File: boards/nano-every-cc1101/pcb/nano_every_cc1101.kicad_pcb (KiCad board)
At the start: 2 copper layers, 100 x 100 mm, 86 parts, among them J1 SMA, J2 SMA, J3 Breakout 1-15, J4 Breakout 16-30, U1 CC1101RGPR, U2 XC6206P332MR, U3 TXS0108EPWR, U501 CC1101RGPR, Y1 26MHz, Y501 26MHz

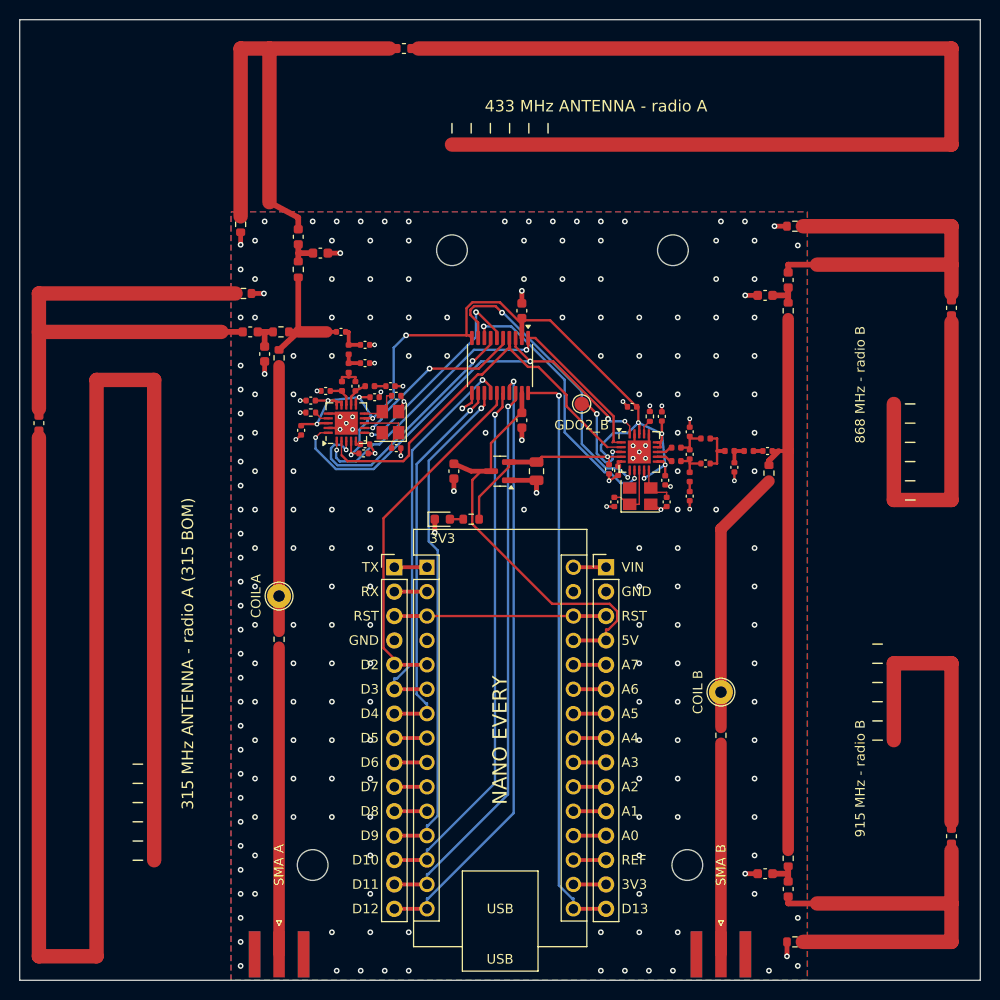
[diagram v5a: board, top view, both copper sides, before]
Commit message: nano-every-cc1101 v2: 70 x 45 mm board with JLCPCB-assembled coil antennas
- Printed IFAs replaced by four helical spring antennas (BAT WIRELESS
  BWxxxSNX, 315/433/868/915 MHz, LCSC C496553-C496556), all fitted and
  assembled; one 0R selector per radio picks the band, each branch keeps a
  T-match for retuning, SMA jacks stay as a hand-fit option.
- Board shrinks from 100 x 100 to 70 x 45 mm: radios stacked beside the
  Nano, TXS0108E rotated so its 5 V side faces the Nano.
- DRC now 0 violations / 0 unconnected: footprint silk clipped off pads
  and the board edge, C41/C51 moved so the DCOUPL cap clears the QFN body,
  a .kicad_dru rule for the intentional QFN-courtyard contacts, ground
  corridors kept open for the CC1101 exposed pads, ground-island joining,
  orphan via stubs removed.
- Docs rewritten for the coil version; antenna/ kept as the v1 study.

Co-Authored-By: Claude Opus 5.5 <noreply@anthropic.com>
Claude-Session: https://claude.ai/code/session_019aUkwoH7eUuCGWSrK9KSBc
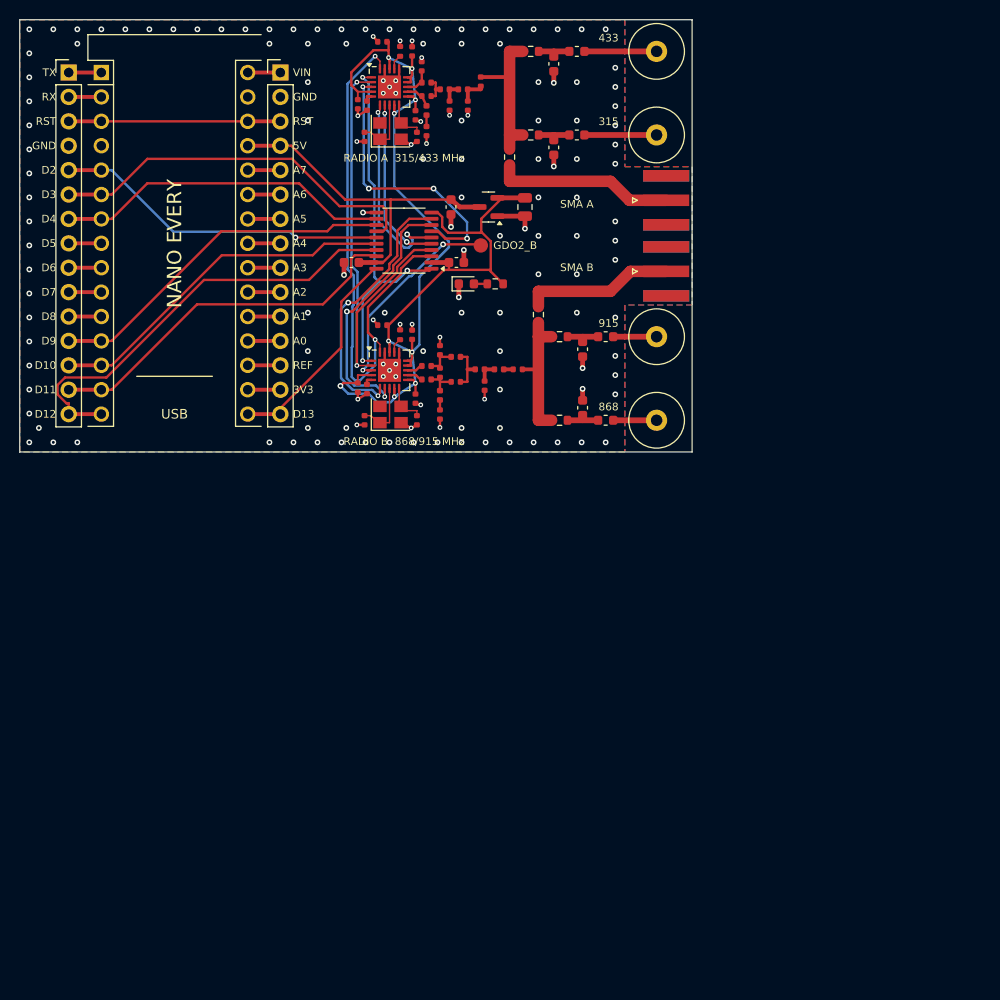
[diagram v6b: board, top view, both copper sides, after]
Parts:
- removed H1, H2: coil, TestPoint:TestPoint_THTPad_D2.5mm_Drill1.2mm
- removed H3, H4, H5, H6: M3, MountingHole:MountingHole_3.2mm_M3
- removed L401: 47pF, Inductor_SMD:L_0603_1608Metric
- removed L402: DNP (39nH to use), Inductor_SMD:L_0603_1608Metric
- removed L404, L405: 0R, Inductor_SMD:L_0603_1608Metric
- removed R401, R402, R404, R405: 0R, Resistor_SMD:R_0603_1608Metric
- removed R407, R408: DNP, Resistor_SMD:R_0603_1608Metric
- added AE1: BW433SNX21-5W2, nano_every_cc1101:Coil_Spring_D5.5_THT, F.Cu at (166.3, 103.3)
- added AE2: BW315SNX39-6W3, nano_every_cc1101:Coil_Spring_D5.5_THT, F.Cu at (166.3, 112.0)
- added AE3: BW868SNX20-5Z6, nano_every_cc1101:Coil_Spring_D5.5_THT, F.Cu at (166.3, 141.7)
- added AE4: BW915SNX17-5W2, nano_every_cc1101:Coil_Spring_D5.5_THT, F.Cu at (166.3, 133.0)
- C301, C321, C331: value 3pF -> DNP
- C311: value 47pF -> DNP
- L301, L321: value 6pF -> 0R
- L311: value 18pF -> 0R
- L331: value 3pF -> 0R
- R311, R331: value DNP (0R to use) -> DNP
- moved J1 88.2 mm to (167.3, 118.8), turned to 0 degrees
- moved J2 71.3 mm to (167.3, 126.2), turned to 0 degrees
- moved A1 61.7 mm to (108.5, 105.5)
- moved J3 61.7 mm to (105.1, 105.5)
- moved J4 61.7 mm to (127.1, 105.5)
- moved L331 60.6 mm to (161.0, 133.0), turned to 0 degrees
- moved R331 59.3 mm to (156.2, 133.0), turned to 0 degrees
- moved C331 57.8 mm to (158.6, 134.3), turned to 90 degrees
- moved C181 41.3 mm to (137.8, 102.3), turned to 0 degrees
- moved L311 39.7 mm to (158.0, 112.0)
- moved R171 38.7 mm to (139.6, 103.3), turned to 90 degrees
- moved C151 37.9 mm to (140.8, 103.3), turned to 90 degrees
- moved C311 37.0 mm to (155.6, 113.3)
- moved C41 36.4 mm to (135.2, 108.8), turned to 90 degrees
- moved U1 35.3 mm to (138.5, 107.0), turned to 0 degrees
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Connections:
- C301 pad 1: M_433 -> GND
- C301 pad 2: GND -> M_433
- C321 pad 1: GND -> M_868
- C321 pad 2: M_868 -> GND
- L311 pad 1: FEED_315 -> M_315
- L311 pad 2: M_315 -> FEED_315
- L331 pad 1: FEED_915 -> M_915
- L331 pad 2: M_915 -> FEED_915
- R311 pad 1: M_315 -> ANT_A
- R311 pad 2: ANT_A -> M_315
- R331 pad 1: M_915 -> ANT_B
- R331 pad 2: ANT_B -> M_915
- R403 pad 1: EXT_A -> SMA_A
- R406 pad 1: EXT_B -> ANT_B
- R406 pad 2: ANT_B -> SMA_B
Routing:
- net ARM_315: track 176.7 -> 0.00 mm
- net ARM_433: track 118.2 -> 0.00 mm
- net FEED_315: track 54.4 -> 7.51 mm
- net FEED_433: track 54.3 -> 7.51 mm
- net ANT_B: track 58.9 -> 14.6 mm
- net FEED_915: track 43.4 -> 4.51 mm
- net D13_SCK: track 60.8 -> 23.1 mm, vias 1 -> 0
- net FEED_868: track 41.0 -> 4.51 mm
- net ARM_868: track 35.2 -> 0.00 mm
- net ARM_915: track 31.2 -> 0.00 mm
- net EXT_B: track 27.7 -> 0.00 mm
- net EXT_A: track 27.7 -> 0.00 mm
- net D11_MOSI: track 58.5 -> 38.9 mm, vias 1 -> 0
- net D10: track 55.4 -> 37.3 mm, vias 1 -> 0
- net D12_MISO: track 63.5 -> 46.1 mm, vias 1 -> 0
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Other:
- board size 100 x 100 mm -> 70 x 45 mm
- board text added: "2-layer 70 x 45 mm v2.0 coil antennas"
- board text added: "315"
- board text added: "433"
- board text added: "868"
- board text added: "915"
- board text added: "A: 433 coil R301 | 315 coil R311 | SMA R403"
- board text added: "A: CSn D10 GDO0 D2 GDO2 D3"
- board text added: "ANTENNA - fit ONE selector per radio"
- board text added: "B: 868 coil R321 | 915 coil R331 | SMA R406"
- board text added: "B: CSn D9 GDO0 D4 GDO2 pad"
- board text added: "RADIO A 315/433 MHz"
- board text added: "RADIO B 868/915 MHz"
- board text added: "coil retune: C3x1 shunt, L3x1 series"
- board text removed: "2-layer 100 x 100 mm v1.0"
- board text removed: "315 MHz ANTENNA - radio A (315 BOM)"
- board text removed: "433 MHz ANTENNA - radio A"
- board text removed: "868 MHz - radio B"
- board text removed: "915 MHz - radio B"
- board text removed: "ANTENNA SELECT - fit ONE selector per radio"
- board text removed: "ANY FREQUENCY 300-348/387-464/779-928 MHz:"
- board text removed: "COIL A"
- board text removed: "COIL B"
- board text removed: "IFA shorts R401 R402 R404 R405: always 0R"
- board text removed: "USB"
- board text removed: "coil in H1/H2: BAT WIRELESS BWxxxSNX spring"
- board text removed: "fit tune L40x + R3x1/C3x1/L3x1 per tuning.md"
- board text removed: "radio A: 433 R301 | 315 R311 | coil R403 | SMA +R407"
- board text removed: "radio A: CSn D10 GDO0 D2 GDO2 D3"
- board text removed: "radio B: 868 R321 | 915 R331 | coil R406 | SMA +R408"
- board text removed: "radio B: CSn D9 GDO0 D4 GDO2 pad"

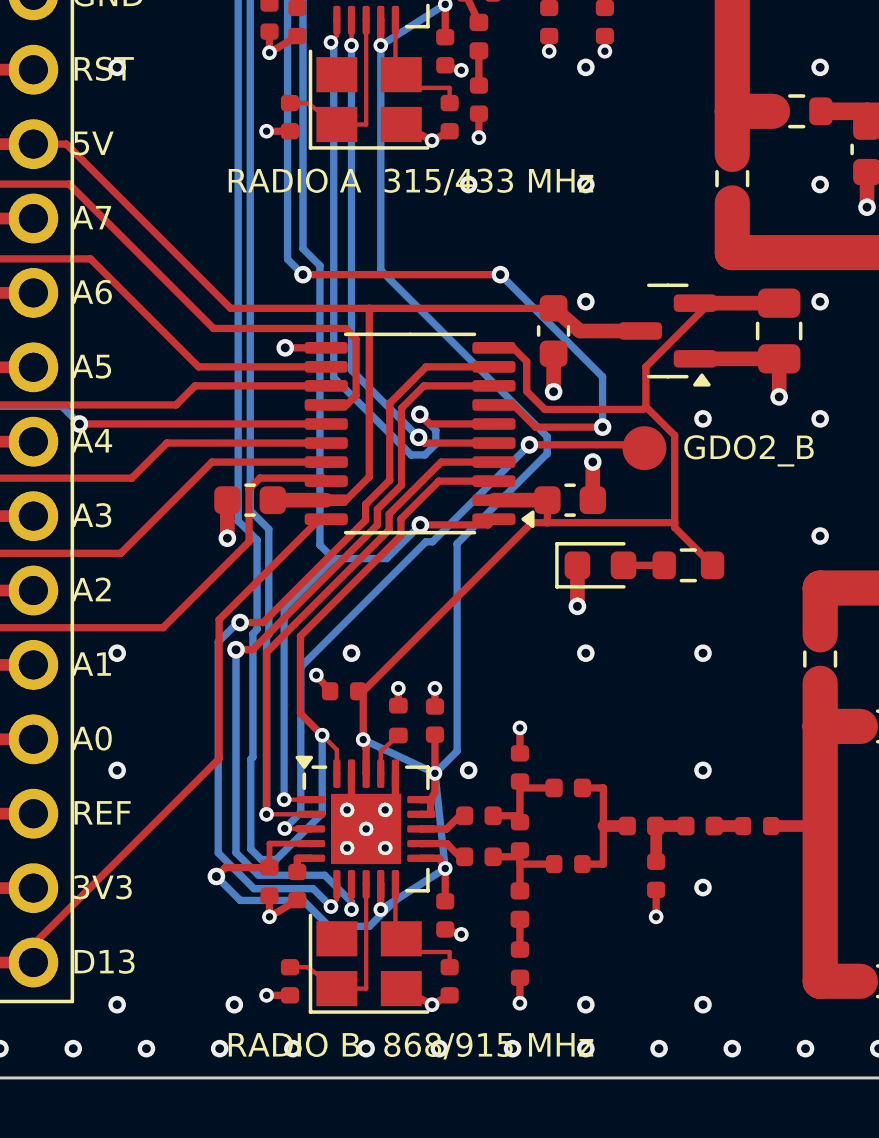
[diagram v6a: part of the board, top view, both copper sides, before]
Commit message: nano-every-cc1101: clean Gerber export for fab upload tools
- Protel extensions (.GTL/.GBL/.GTS/.GBS/.GTP/.GTO/.GBO/.GM1), silkscreen
  clipped by the soldermask, explicit mm/decimal Excellon.
- Drop the drill-map drawings and the empty NPTH drill file, which upload
  tools misread as layers / reject.
- Keep ground-stitching vias out of the board labels ('RADIO B' was cut).
Checked with an independent parser (gerbonara): all layers identified,
239 drill hits = 175 vias + 64 THT pads, 70 x 45 mm outline; DRC 0/0.

Co-Authored-By: Claude Opus 5.5 <noreply@anthropic.com>
Claude-Session: https://claude.ai/code/session_019aUkwoH7eUuCGWSrK9KSBc
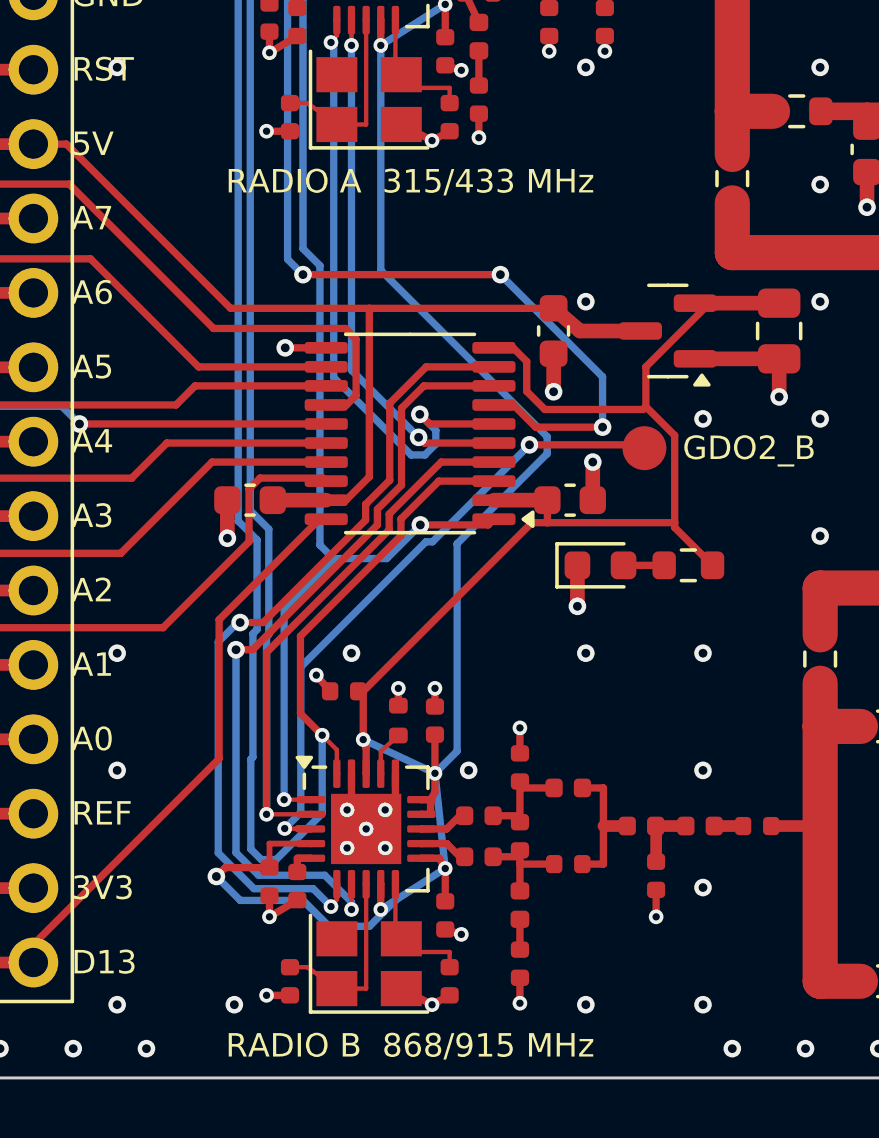
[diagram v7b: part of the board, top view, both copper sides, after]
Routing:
- net GND: vias 153 -> 144
